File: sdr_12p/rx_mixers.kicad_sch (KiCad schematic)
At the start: 0 parts

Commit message: basic arrangement of blocks
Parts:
- added U6: 74CBT1G125DBVRE4, DBV5, symbol SN74CBT1G125:74CBT1G125DBVRE4
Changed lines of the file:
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@@
 		(company "Andy McCann KA3KAF and Doug McCann KA3KAG")
 	)
+	(symbol
+		(lib_id "SN74CBT1G125:74CBT1G125DBVRE4")
+		(at 63.5 40.64 0)
+		(unit 1)
+		(exclude_from_sim no)
+		(in_bom yes)
+		(on_board yes)
+		(dnp no)
+		(fields_autoplaced yes)
+		(property "Reference" "U6"
+			(at 91.44 30.48 0)
+			(effects
+				(font
+					(size 1.524 1.524)
+				)
+			)
+		)
+		(property "Value" "74CBT1G125DBVRE4"
+			(at 91.44 33.02 0)
+			(effects
+				(font
+					(size 1.524 1.524)
+				)
+			)
+		)
+		(property "Footprint" "DBV5"
+			(at 63.5 40.64 0)
+			(effects
+				(font
+					(size 1.27 1.27)
+					(italic yes)
+				)
+				(hide yes)
+			)
+		)
+		(property "Datasheet" "https://www.ti.com/lit/gpn/sn74cbt1g125"
+			(at 63.5 40.64 0)
+			(effects
+				(font
+					(size 1.27 1.27)
+					(italic yes)
+				)
+				(hide yes)
+			)
+		)
+		(property "Description" ""
+			(at 63.5 40.64 0)
+			(effects
+				(font
+					(size 1.27 1.27)
+				)
+				(hide yes)
+			)
+		)
+		(pin "5"
+		)
+		(pin "1"
+		)
+		(pin "3"
+		)
+		(pin "2"
+		)
+		(pin "4"
+		)
+		(instances
+			(project ""
+				(path "/fe42ca2f-2bb8-4d5a-9e84-807788ed632f/d923ed07-1122-4091-b99e-c24c264ea9d2"
+					(reference "U6")
+					(unit 1)
+				)
+			)
+		)
+	)
 )

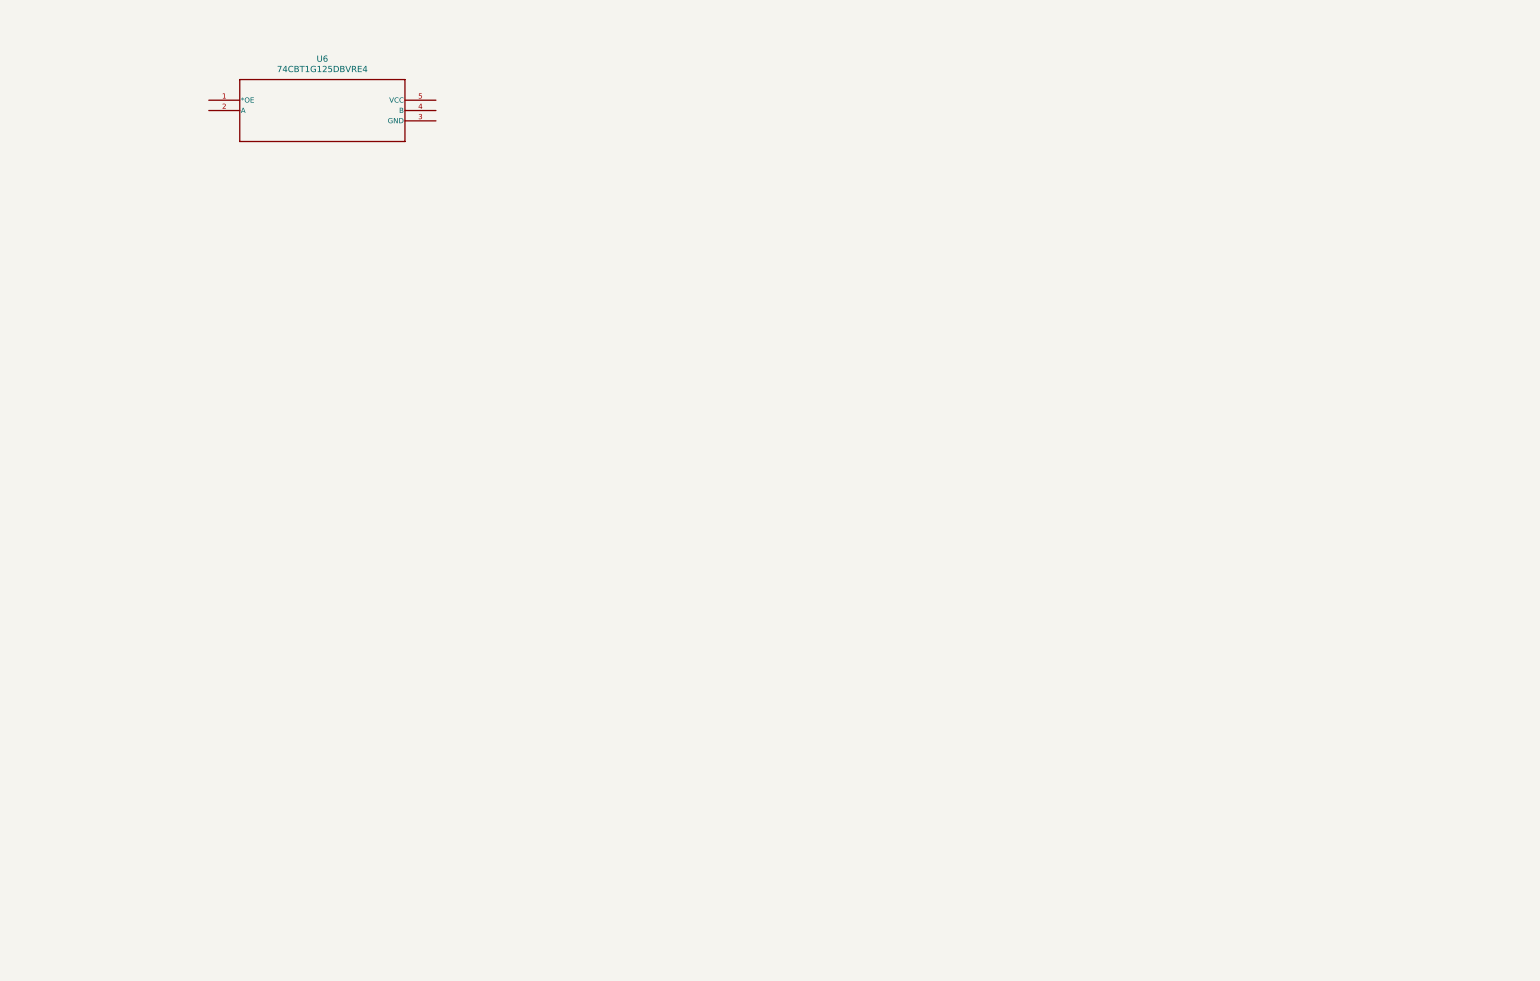
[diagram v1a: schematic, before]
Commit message: added rx switches
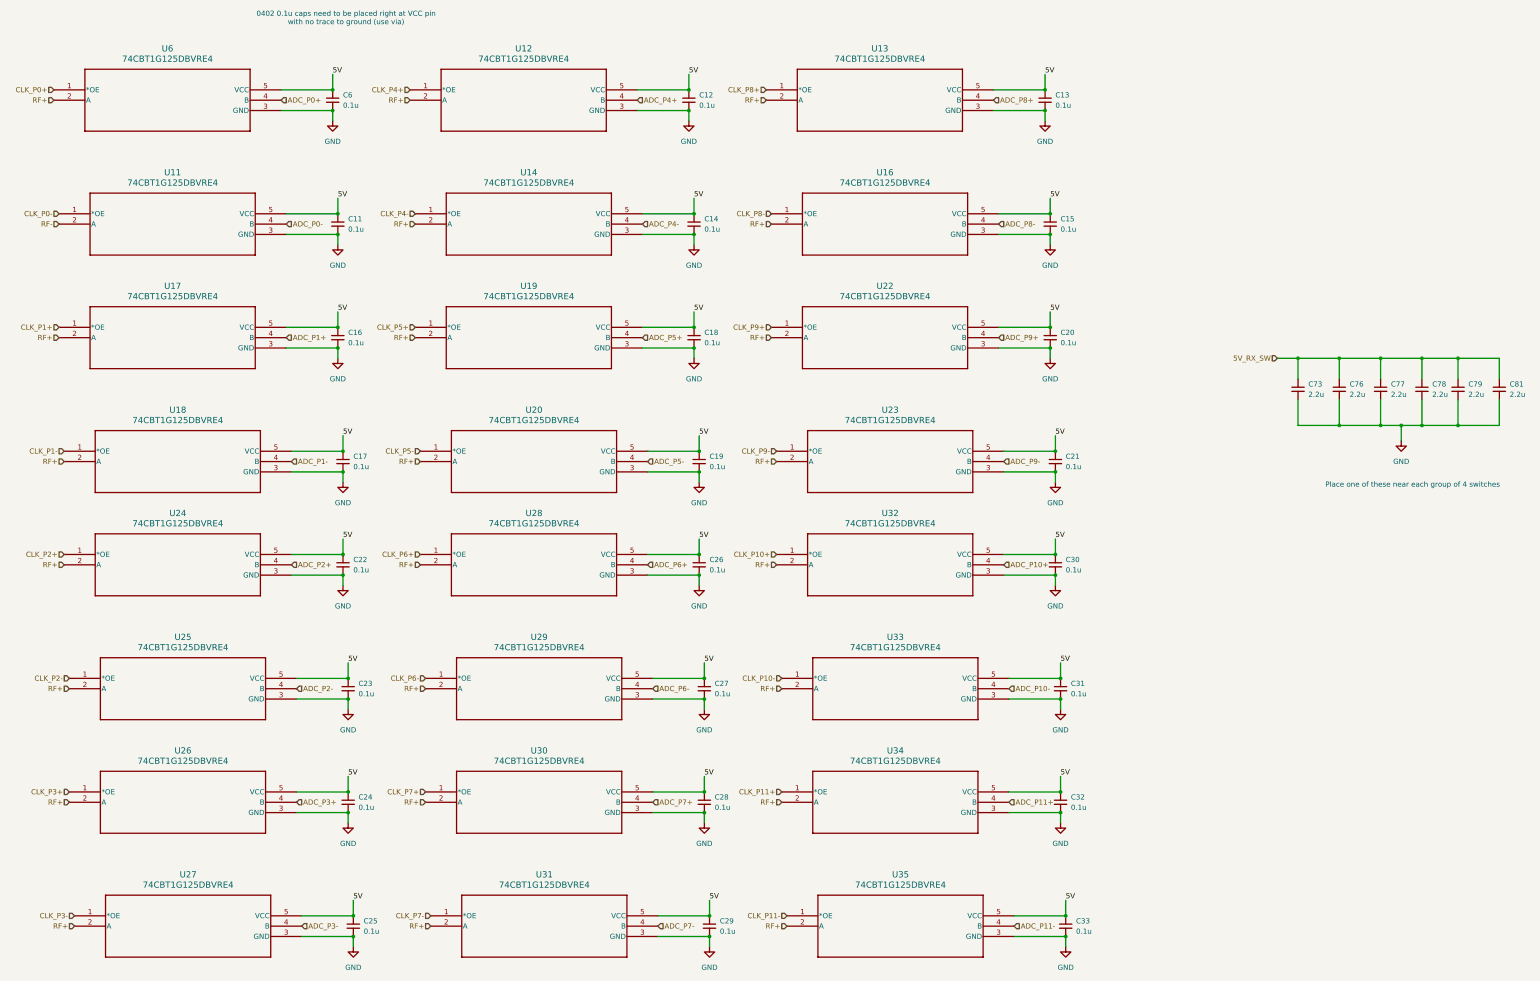
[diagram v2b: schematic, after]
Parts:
- added C11, C12, C13, C14, C15, C16, C17, C18, C19, C20, C21, C22, C23, C24, C25, C26, C27, C28, C29, C30, C31, C32, C33, C6: 0.1u, Resistor_SMD:R_0402_1005Metric_Pad0.72x0.64mm_HandSolder, symbol Device:C_Small
- added C73, C76, C77, C78, C79, C81: 2.2u, symbol Device:C_Small
- added U11, U12, U13, U14, U16, U17, U18, U19, U20, U22, U23, U24, U25, U26, U27, U28, U29, U30, U31, U32, U33, U34, U35: 74CBT1G125DBVRE4, DBV5, symbol SN74CBT1G125:74CBT1G125DBVRE4
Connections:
- net CLK_P0+: now reaches U6.1 (*OE)
- net RF+: now reaches U6.2 (A)
- net RF+: now also U12.2 (A), U13.2 (A), U14.2 (A), U16.2 (A), U17.2 (A), U18.2 (A), U19.2 (A), U20.2 (A), U22.2 (A), U23.2 (A), U24.2 (A), U25.2 (A), U26.2 (A), U27.2 (A), U28.2 (A), U29.2 (A), U30.2 (A), U31.2 (A), U32.2 (A), U33.2 (A), U34.2 (A), U35.2 (A)
- net GND: now reaches U6.3 (GND)
- net GND: now also C11.2, C12.2, C13.2, C14.2, C15.2, C16.2, C17.2, C18.2, C19.2, C20.2, C21.2, C22.2, C23.2, C24.2, C25.2, C26.2, C27.2, C28.2, C29.2, C30.2, C31.2, C32.2, C33.2, C6.2, C73.2, C76.2, C77.2, C78.2, C79.2, C81.2, U11.3 (GND), U12.3 (GND), U13.3 (GND), U14.3 (GND), U16.3 (GND), U17.3 (GND), U18.3 (GND), U19.3 (GND), U20.3 (GND), U22.3 (GND), U23.3 (GND), U24.3 (GND), U25.3 (GND), U26.3 (GND), U27.3 (GND), U28.3 (GND), U29.3 (GND), U30.3 (GND), U31.3 (GND), U32.3 (GND), U33.3 (GND), U34.3 (GND), U35.3 (GND)
- net ADC_P0+: now reaches U6.4 (B)
- net 5V: now reaches U6.5 (VCC)
- net 5V: now also C11.1, C12.1, C13.1, C14.1, C15.1, C16.1, C17.1, C18.1, C19.1, C20.1, C21.1, C22.1, C23.1, C24.1, C25.1, C26.1, C27.1, C28.1, C29.1, C30.1, C31.1, C32.1, C33.1, C6.1, U11.5 (VCC), U12.5 (VCC), U13.5 (VCC), U14.5 (VCC), U16.5 (VCC), U17.5 (VCC), U18.5 (VCC), U19.5 (VCC), U20.5 (VCC), U22.5 (VCC), U23.5 (VCC), U24.5 (VCC), U25.5 (VCC), U26.5 (VCC), U27.5 (VCC), U28.5 (VCC), U29.5 (VCC), U30.5 (VCC), U31.5 (VCC), U32.5 (VCC), U33.5 (VCC), U34.5 (VCC), U35.5 (VCC)
- new net 5V_RX_SW: C73.1, C76.1, C77.1, C78.1, C79.1, C81.1
- new net ADC_P0-: U11.4 (B)
- new net ADC_P1+: U17.4 (B)
- new net ADC_P1-: U18.4 (B)
- new net ADC_P10+: U32.4 (B)
- new net ADC_P10-: U33.4 (B)
- new net ADC_P11+: U34.4 (B)
- new net ADC_P11-: U35.4 (B)
- new net ADC_P2+: U24.4 (B)
- new net ADC_P2-: U25.4 (B)
- new net ADC_P3+: U26.4 (B)
- new net ADC_P3-: U27.4 (B)
- new net ADC_P4+: U12.4 (B)
- new net ADC_P4-: U14.4 (B)
- new net ADC_P5+: U19.4 (B)
- new net ADC_P5-: U20.4 (B)
- new net ADC_P6+: U28.4 (B)
- new net ADC_P6-: U29.4 (B)
- new net ADC_P7+: U30.4 (B)
- new net ADC_P7-: U31.4 (B)
- new net ADC_P8+: U13.4 (B)
- new net ADC_P8-: U16.4 (B)
- new net ADC_P9+: U22.4 (B)
- new net ADC_P9-: U23.4 (B)
- new net CLK_P0-: U11.1 (*OE)
- new net CLK_P1+: U17.1 (*OE)
- new net CLK_P1-: U18.1 (*OE)
- new net CLK_P10+: U32.1 (*OE)
- new net CLK_P10-: U33.1 (*OE)
- new net CLK_P11+: U34.1 (*OE)
- new net CLK_P11-: U35.1 (*OE)
- new net CLK_P2+: U24.1 (*OE)
- new net CLK_P2-: U25.1 (*OE)
- new net CLK_P3+: U26.1 (*OE)
- new net CLK_P3-: U27.1 (*OE)
- new net CLK_P4+: U12.1 (*OE)
- new net CLK_P4-: U14.1 (*OE)
- new net CLK_P5+: U19.1 (*OE)
- new net CLK_P5-: U20.1 (*OE)
- new net CLK_P6+: U28.1 (*OE)
- new net CLK_P6-: U29.1 (*OE)
- new net CLK_P7+: U30.1 (*OE)
- new net CLK_P7-: U31.1 (*OE)
- new net CLK_P8+: U13.1 (*OE)
- new net CLK_P8-: U16.1 (*OE)
- new net CLK_P9+: U22.1 (*OE)
- new net CLK_P9-: U23.1 (*OE)
- new net RF-: U11.2 (A)
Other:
- note added: "0402 0.1u caps need to be placed right at VCC pin with no trace to ground (use via)"
- note added: "Place one of these near each group of 4 switches"
- moved on the sheet: U6

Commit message: updated rx mixer page
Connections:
- net 5V renamed 5V_RX_Mixer
- net 5V_RX_Mixer: no longer C22.1, U24.5 (VCC)
- new net: C22.1, U24.5 (VCC)
